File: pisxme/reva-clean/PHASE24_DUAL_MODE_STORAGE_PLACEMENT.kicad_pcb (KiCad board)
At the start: 6 copper layers, 300 x 180 mm, 95 parts, among them J1 74221-101LF, J2 A70-112-331N126, J3 1-2199230-4, J4 Amphenol 10171746-00021LF USB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, J5 0039300020, J6 0039300020, J7 Raspberry-Pi-5-Compute-Module, Q1 CSD19536KCS, Q2 CSD19536KCS, U1 LM74700QDBVRQ1, U2 LM74700QDBVRQ1, U3 TPSM63606RDLR, U4 TPSM63606RDLR, U5 TPSM63606RDLR, U6 TPD4EUSB30, U7 TUSB9261IPVP, U8 Texas_DRT_3, U9 TPD4EUSB30

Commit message: phase24 add PEDET mode control authority
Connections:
- net CM5_USB2_DN renamed CM5_USB2_DM
- net CM5_USB3_RXN renamed CM5_SSRXN
- net CM5_USB3_RXP renamed CM5_SSRXP
- net CM5_USB3_TXN renamed CM5_SSTXN
- net CM5_USB3_TXP renamed CM5_SSTXP
- net GND renamed TME
- net JMS_CLKREQ_N renamed PCIE_CLKREQ_N
- net JMS_LXO renamed LXO
- net JMS_PERST_N renamed PCIE_RESET_N
- net JMS_REFCLK_N renamed REFCLK_N
- net JMS_REFCLK_P renamed REFCLK_P
- net JMS_USB2_DN renamed JMS_USB2_DM
- net JMS_USB3_RXN renamed JMS_SSRXN
- net JMS_USB3_RXP renamed JMS_SSRXP
- net JMS_USB3_TXN renamed JMS_SSTXN
- net JMS_USB3_TXP renamed JMS_SSTXP
- net JMS_USB_RXN1 renamed USB_RXN1
- net JMS_USB_RXN2 renamed USB_RXN2
- net JMS_USB_RXP1 renamed USB_RXP1
- net JMS_USB_RXP2 renamed USB_RXP2
- net JMS_USB_TXN1 renamed USB_TXN1
- net JMS_USB_TXN2 renamed USB_TXN2
- net JMS_USB_TXP1 renamed USB_TXP1
- net JMS_USB_TXP2 renamed USB_TXP2
- net JMS_XIN renamed XIN
- net JMS_XOUT renamed XOUT
- net STORAGE_USB_DN renamed USB_DM
- net STORAGE_USB_DP renamed USB_DP
- net STORAGE_USB_SEL renamed USB_SEL
- net STORAGE_USB_VBUS renamed VBUS
- net TUSB_USB2_DN renamed TUSB_USB2_DM
- net TUSB_USB3_RXN renamed TUSB_SSRXN
- net TUSB_USB3_RXP renamed TUSB_SSRXP
- net TUSB_USB3_TXN renamed TUSB_SSTXN
- net TUSB_USB3_TXP renamed TUSB_SSTXP
- net USB_SEL_OE_N renamed USB_OE_N
- J3 pad 1: (no net) -> M2_CONFIG3
- J3 pad 10: (no net) -> M2_DAS_DSS
- J3 pad 11: (no net) -> M2_PCIE_TXN3
- J3 pad 12: (no net) -> M2_3V3
- J3 pad 13: (no net) -> M2_PCIE_TXP3
- J3 pad 14: (no net) -> M2_3V3
- J3 pad 15: (no net) -> M2_GND
- J3 pad 16: (no net) -> M2_3V3
- J3 pad 17: (no net) -> M2_PCIE_RXN2
- J3 pad 18: (no net) -> M2_3V3
- J3 pad 19: (no net) -> M2_PCIE_RXP2
- J3 pad 21: (no net) -> M2_CONFIG0
- J3 pad 23: (no net) -> M2_PCIE_TXN2
- J3 pad 25: (no net) -> M2_PCIE_TXP2
- J3 pad 27: (no net) -> M2_GND
- J3 pad 29: (no net) -> M2_PCIE_RXN1
- J3 pad 3: POWER_GND -> M2_GND
- J3 pad 31: (no net) -> M2_PCIE_RXP1
- J3 pad 33: (no net) -> M2_GND
- J3 pad 35: (no net) -> M2_PCIE_TXN1
- J3 pad 37: (no net) -> M2_PCIE_TXP1
- J3 pad 38: (no net) -> M2_DEVSLP
- J3 pad 39: (no net) -> M2_GND
- J3 pad 45: (no net) -> M2_GND
- J3 pad 5: (no net) -> M2_PCIE_RXN3
- J3 pad 51: (no net) -> M2_GND
- J3 pad 56: (no net) -> M2_MFG1
- J3 pad 57: (no net) -> M2_GND
- J3 pad 58: (no net) -> M2_MFG2
- J3 pad 69: (no net) -> M2_PEDET
- J3 pad 7: (no net) -> M2_PCIE_RXP3
- J3 pad 71: POWER_GND -> M2_GND
- J3 pad 73: POWER_GND -> M2_GND
- J3 pad 75: (no net) -> M2_CONFIG2
- J3 pad 9: (no net) -> M2_GND
- U11 pad 1: (no net) -> JMS_VDDREG_5V
- U11 pad 10: (no net) -> JMS_VBUS_SENSE
- U11 pad 11: (no net) -> JMS_VCCO
- U11 pad 12: (no net) -> JMS_GPIO7_NC
- U11 pad 13: (no net) -> JMS_GPIO8_NC
- U11 pad 14: (no net) -> JMS_GPIO9_NC
- U11 pad 15: (no net) -> JMS_RESET_N
- U11 pad 19: (no net) -> JMS_AVDD33
- U11 pad 2: (no net) -> JMS_VCCK
- U11 pad 20: (no net) -> JMS_AVDDL
- U11 pad 25: (no net) -> JMS_AVDDL
- U11 pad 3: (no net) -> JMS_SPI_SO_DNP
- U11 pad 30: (no net) -> JMS_AVDDL
- U11 pad 31: (no net) -> JMS_VCCK
- U11 pad 32: (no net) -> JMS_VCCO
- U11 pad 33: (no net) -> JMS_AVDDL
- U11 pad 34: JMS_PCIE_RXN1 -> PCIE_RXN1
- U11 pad 35: JMS_PCIE_RXP1 -> PCIE_RXP1
- U11 pad 36: (no net) -> JMS_AVDDL
- U11 pad 37: JMS_PCIE_TXN1 -> PCIE_TXN1
- U11 pad 38: JMS_PCIE_TXP1 -> PCIE_TXP1
- U11 pad 39: (no net) -> JMS_REXT
- U11 pad 4: (no net) -> JMS_SPI_SCK_DNP
- U11 pad 40: (no net) -> JMS_AVDDL
- U11 pad 41: JMS_PCIE_RXN0 -> PCIE_RXN0
- U11 pad 42: JMS_PCIE_RXP0 -> PCIE_RXP0
- U11 pad 43: (no net) -> JMS_AVDDL
- U11 pad 44: JMS_PCIE_TXN0 -> PCIE_TXN0
- U11 pad 45: JMS_PCIE_TXP0 -> PCIE_TXP0
- U11 pad 46: (no net) -> JMS_AVDDL
- U11 pad 49: (no net) -> JMS_AVDDL
- U11 pad 5: (no net) -> JMS_SPI_SI_DNP
- U11 pad 52: (no net) -> JMS_XAVDDH
- U11 pad 53: (no net) -> JMS_VCCK
- U11 pad 56: (no net) -> JMS_VCCO
- U11 pad 57: (no net) -> JMS_GPIO12_NC
- U11 pad 58: (no net) -> JMS_GPIO11_NC
- U11 pad 59: (no net) -> JMS_GPIO10_NC
- U11 pad 6: (no net) -> JMS_VCCO
- U11 pad 61: (no net) -> JMS_CC2_NC
- U11 pad 62: (no net) -> JMS_CC1_NC
- U11 pad 7: (no net) -> JMS_SPI_CS_N_DNP
- U11 pad 8: (no net) -> JMS_GPIO4_NC
- U11 pad 9: (no net) -> JMS_GPIO5_NC
- U12 pad 14: (no net) -> POWER_GND
- U12 pad 17: (no net) -> POWER_GND
- U12 pad 18: (no net) -> NC_18
- U12 pad 19: (no net) -> POWER_GND
- U12 pad 21: (no net) -> POWER_GND
- U12 pad 35: (no net) -> NC_35
- U12 pad 36: (no net) -> NC_36
- U12 pad 37: (no net) -> NC_37
- U12 pad 38: (no net) -> NC_38
- U12 pad 39: (no net) -> NC_39
- U12 pad 40: (no net) -> NC_40
- U12 pad 41: (no net) -> NC_41
- U12 pad 42: (no net) -> NC_42
- U13 pad 1: (no net) -> POWER_GND
- U13 pad 12: M2_PCIE_RXP2 -> M2_PCIE_TXN2
- U13 pad 13: (no net) -> STORAGE_3V3
- U13 pad 14: (no net) -> POWER_GND
- U13 pad 16: M2_PCIE_RXP3 -> M2_PCIE_TXN3
- U13 pad 17: (no net) -> POWER_GND
- U13 pad 18: (no net) -> NC_18
- U13 pad 19: (no net) -> POWER_GND
- U13 pad 2: M2_PCIE_TXP0 -> M2_SATA_A_P_PCIE_TXP0
- U13 pad 20: (no net) -> STORAGE_3V3
- U13 pad 21: (no net) -> POWER_GND
- U13 pad 22: JMS_PCIE_TXN0 -> JMS_PCIE_RXN1
- U13 pad 23: JMS_PCIE_TXP0 -> JMS_PCIE_RXP1
- U13 pad 24: JMS_PCIE_RXN0 -> JMS_PCIE_TXN1
- U13 pad 25: JMS_PCIE_RXP0 -> JMS_PCIE_TXP1
- U13 pad 26: TUSB_SATA_RXN -> NC_26
- U13 pad 27: TUSB_SATA_RXP -> NC_27
- U13 pad 28: TUSB_SATA_TXN -> NC_28
- U13 pad 29: TUSB_SATA_TXP -> NC_29
- U13 pad 3: M2_PCIE_RXP0 -> M2_SATA_A_N_PCIE_TXN0
- U13 pad 31: (no net) -> JMS_PCIE_RXN0
- U13 pad 32: (no net) -> JMS_PCIE_RXP0
- U13 pad 33: (no net) -> JMS_PCIE_TXN0
- U13 pad 34: (no net) -> JMS_PCIE_TXP0
- U13 pad 35: (no net) -> TUSB_SATA_RXN
- U13 pad 36: (no net) -> TUSB_SATA_RXP
- U13 pad 37: (no net) -> TUSB_SATA_TXN
- U13 pad 38: (no net) -> TUSB_SATA_TXP
- U13 pad 39: (no net) -> NC_39
- U13 pad 4: (no net) -> POWER_GND
- U13 pad 40: (no net) -> NC_40
- U13 pad 41: (no net) -> NC_41
- U13 pad 42: (no net) -> NC_42
- U13 pad 7: M2_PCIE_RXP1 -> M2_PCIE_TXN1
- U13 pad 8: (no net) -> NC_8

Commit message: phase24 add PEDET buffer to storage candidate
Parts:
- added U14: , SOT-23-5, F.Cu at (210.0, 150.0)
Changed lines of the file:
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@@
  (pad "43" smd rect (at 0 0) (size 4.46 4.46) (layers "F.Cu" "F.Paste" "F.Mask"))
 )
+(footprint "SOT-23-5" (version 20240108) (generator pcbnew)
+ (layer "F.Cu")
+ (at 210 150)
+  (descr "TI SN74LVC1G17DBVR; DBV SOT-23-5 review footprint")
+  (property "Reference" "U14" (at 0 -2.4 0) (layer "F.SilkS")
+    (effects (font (size 0.8 0.8) (thickness 0.12))))
+  (property "Value" "" (at 0 2.4 0) (layer "F.Fab") hide
+    (effects (font (size 0.8 0.8))))
+  (attr smd)
+  (fp_rect (start -1.7 -1.4) (end 1.7 1.4)
+    (stroke (width 0.05) (type default)) (fill none) (layer "F.CrtYd"))
+  (fp_line (start -0.9 -0.9) (end -0.45 -0.9)
+    (stroke (width 0.15) (type default)) (layer "F.SilkS"))
+  (fp_line (start -0.9 -0.9) (end -0.9 -0.45)
+    (stroke (width 0.15) (type default)) (layer "F.SilkS"))
+  (pad "1" smd roundrect (at -1.1 -0.95) (size 1.0 0.6) (layers "F.Cu" "F.Paste" "F.Mask") (roundrect_rratio 0.2))
+  (pad "2" smd roundrect (at -1.1 0.0) (size 1.0 0.6) (layers "F.Cu" "F.Paste" "F.Mask") (roundrect_rratio 0.2) (net "M2_PEDET") (pinfunction "M2_PEDET") (pintype "passive"))
+  (pad "3" smd roundrect (at -1.1 0.95) (size 1.0 0.6) (layers "F.Cu" "F.Paste" "F.Mask") (roundrect_rratio 0.2) (net "POWER_GND") (pinfunction "POWER_GND") (pintype "passive"))
+  (pad "4" smd roundrect (at 1.1 0.95) (size 1.0 0.6) (layers "F.Cu" "F.Paste" "F.Mask") (roundrect_rratio 0.2) (net "STORAGE_SEL") (pinfunction "STORAGE_SEL") (pintype "passive"))
+  (pad "5" smd roundrect (at 1.1 -0.95) (size 1.0 0.6) (layers "F.Cu" "F.Paste" "F.Mask") (roundrect_rratio 0.2) (net "STORAGE_3V3") (pinfunction "STORAGE_3V3") (pintype "passive"))
 )
+)

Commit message: phase24 author dual-mode storage support network
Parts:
- added ?: , Crystal_3225_4Pad, F.Cu at (270.0, 190.0)
- added C: C_0603_1608Metric, C_0603_1608Metric, F.Cu at (310.0, 184.0)
- added C: C_0402_1005Metric, C_0402_1005Metric, F.Cu at (310.0, 192.0)
- added C: C_0402_1005Metric, C_0402_1005Metric, F.Cu at (315.0, 192.0)
- added C: C_0402_1005Metric, C_0402_1005Metric, F.Cu at (320.0, 192.0)
- added C: C_0402_1005Metric, C_0402_1005Metric, F.Cu at (325.0, 192.0)
- added C: C_0402_1005Metric, C_0402_1005Metric, F.Cu at (300.0, 196.0)
- added C: C_0402_1005Metric, C_0402_1005Metric, F.Cu at (315.0, 184.0)
- added C: C_0402_1005Metric, C_0402_1005Metric, F.Cu at (320.0, 184.0)
- added C: C_0402_1005Metric, C_0402_1005Metric, F.Cu at (325.0, 184.0)
- added C: C_0402_1005Metric, C_0402_1005Metric, F.Cu at (300.0, 188.0)
- added C: C_0402_1005Metric, C_0402_1005Metric, F.Cu at (310.0, 188.0)
- added C: C_0402_1005Metric, C_0402_1005Metric, F.Cu at (325.0, 188.0)
- added C: C_0402_1005Metric, C_0402_1005Metric, F.Cu at (300.0, 192.0)
- added C: C_0402_1005Metric, C_0402_1005Metric, F.Cu at (305.0, 192.0)
- added J4: , MODE_JUMPER_1x04, F.Cu at (230.0, 165.0)
- added L2: 4.7uH, L_2520_6332Metric, F.Cu at (258.0, 180.0)
- added R34: R_0402_1005Metric, R_0402_1005Metric, F.Cu at (250.0, 180.0)
- added R35: R_0402_1005Metric, R_0402_1005Metric, F.Cu at (305.0, 188.0)
- added R36: R_0402_1005Metric, R_0402_1005Metric, F.Cu at (315.0, 188.0)
- added R37: R_0402_1005Metric, R_0402_1005Metric, F.Cu at (320.0, 188.0)
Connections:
- U11 pad 60: TME -> POWER_GND
- U14 pad 2: M2_PEDET -> MODE_IN

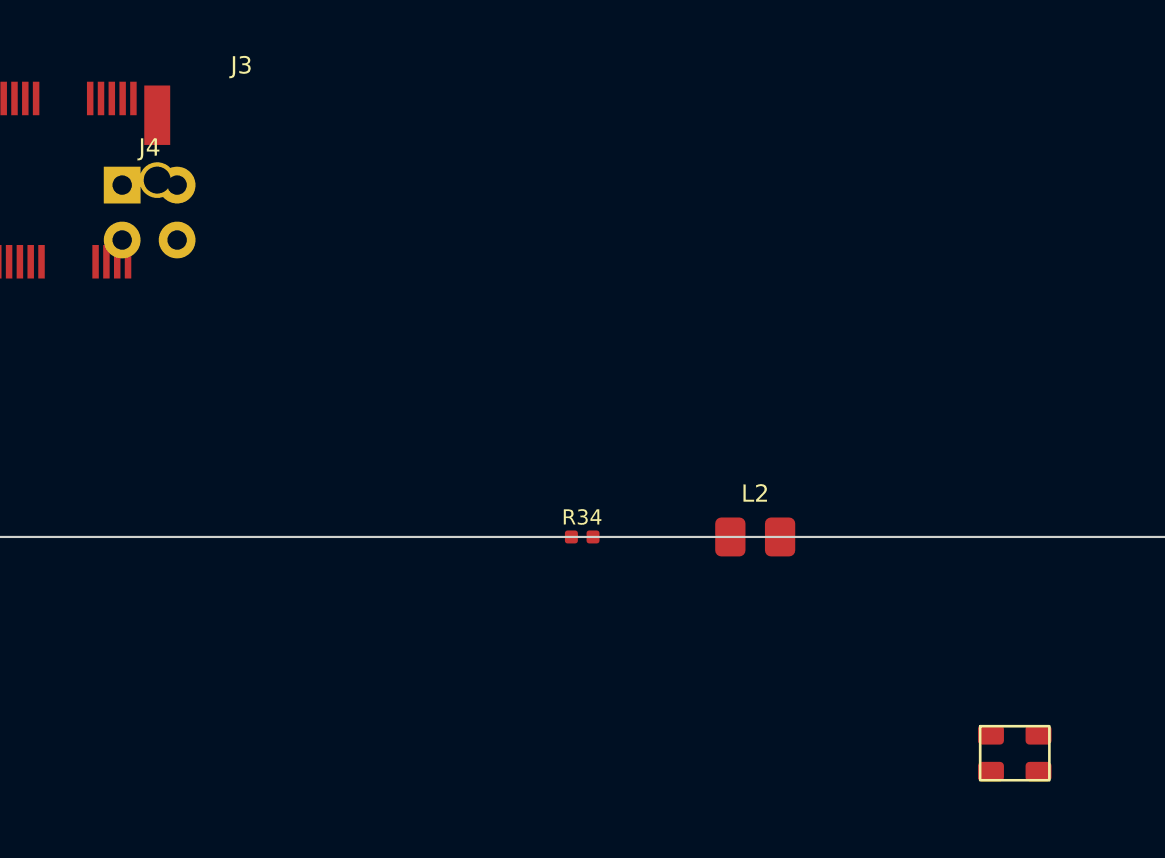
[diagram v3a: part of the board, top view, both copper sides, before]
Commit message: phase24 correct storage mode reference collision
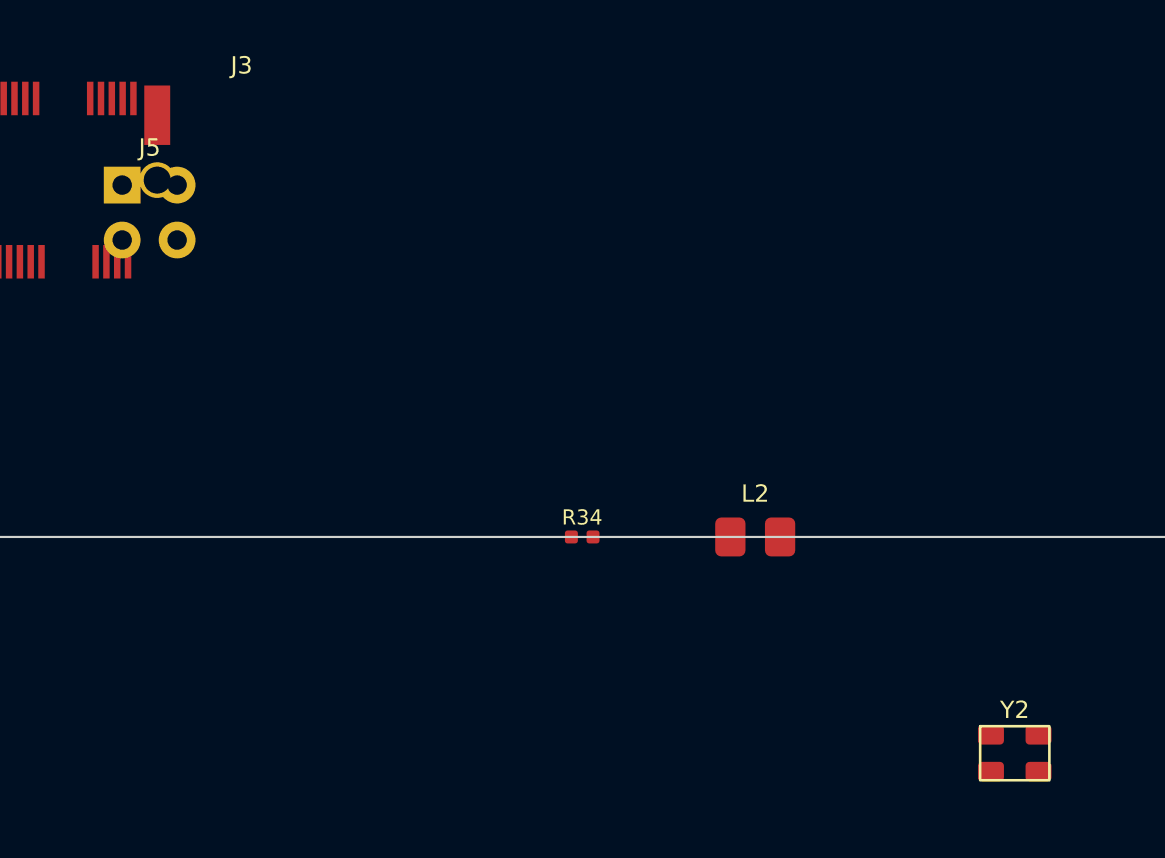
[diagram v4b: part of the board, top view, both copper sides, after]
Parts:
- removed the J4 at (230.0, 165.0)
- added J5: , MODE_JUMPER_1x04, F.Cu at (230.0, 165.0)
- Y2: renamed from ?; value (none) -> 25MHz
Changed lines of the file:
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@@
  (at 230 165)
   (descr "Storage-local power-off mode strap: FORCE_SATA/AUTO_PEDET/FORCE_NVME/MODE_IN")
-  (property "Reference" "J4" (at 0 -3 0) (layer "F.SilkS")
+  (property "Reference" "J5" (at 0 -3 0) (layer "F.SilkS")
     (effects (font (size 0.8 0.8) (thickness 0.12))))
   (property "Value" "" (at 0 3 0) (layer "F.Fab") hide (effects (font (size 0.8 0.8))))
@@
  (at 270 190)
   (descr "3.2 x 2.5 mm 4-pad crystal; verify vendor pad numbering before release")
+  (property "Reference" "Y2" (at 0 -2.0) (layer "F.SilkS") (effects (font (size 0.8 0.8) (thickness 0.12))))
+  (property "Value" "25MHz" (at 0 2.0) (layer "F.Fab") hide (effects (font (size 0.8 0.8))))
   (fp_rect (start -1.6 -1.25) (end 1.6 1.25) (stroke (width 0.12) (type default)) (fill none) (layer "F.SilkS"))
   (fp_rect (start -1.7 -1.35) (end 1.7 1.35) (stroke (width 0.05) (type default)) (fill none) (layer "F.CrtYd"))
